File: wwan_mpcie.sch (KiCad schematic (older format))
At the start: 39 parts, among them J1501 u.FL, J1502 u.FL, J1503 MPCIE-Socket, J1504 Mini_SIM_Card, Q1501 FDV301N, SW1501 WWAN_HKS, U1501 NTB0104GU12, U1502 NUP5120, U1503 74LVC1G08

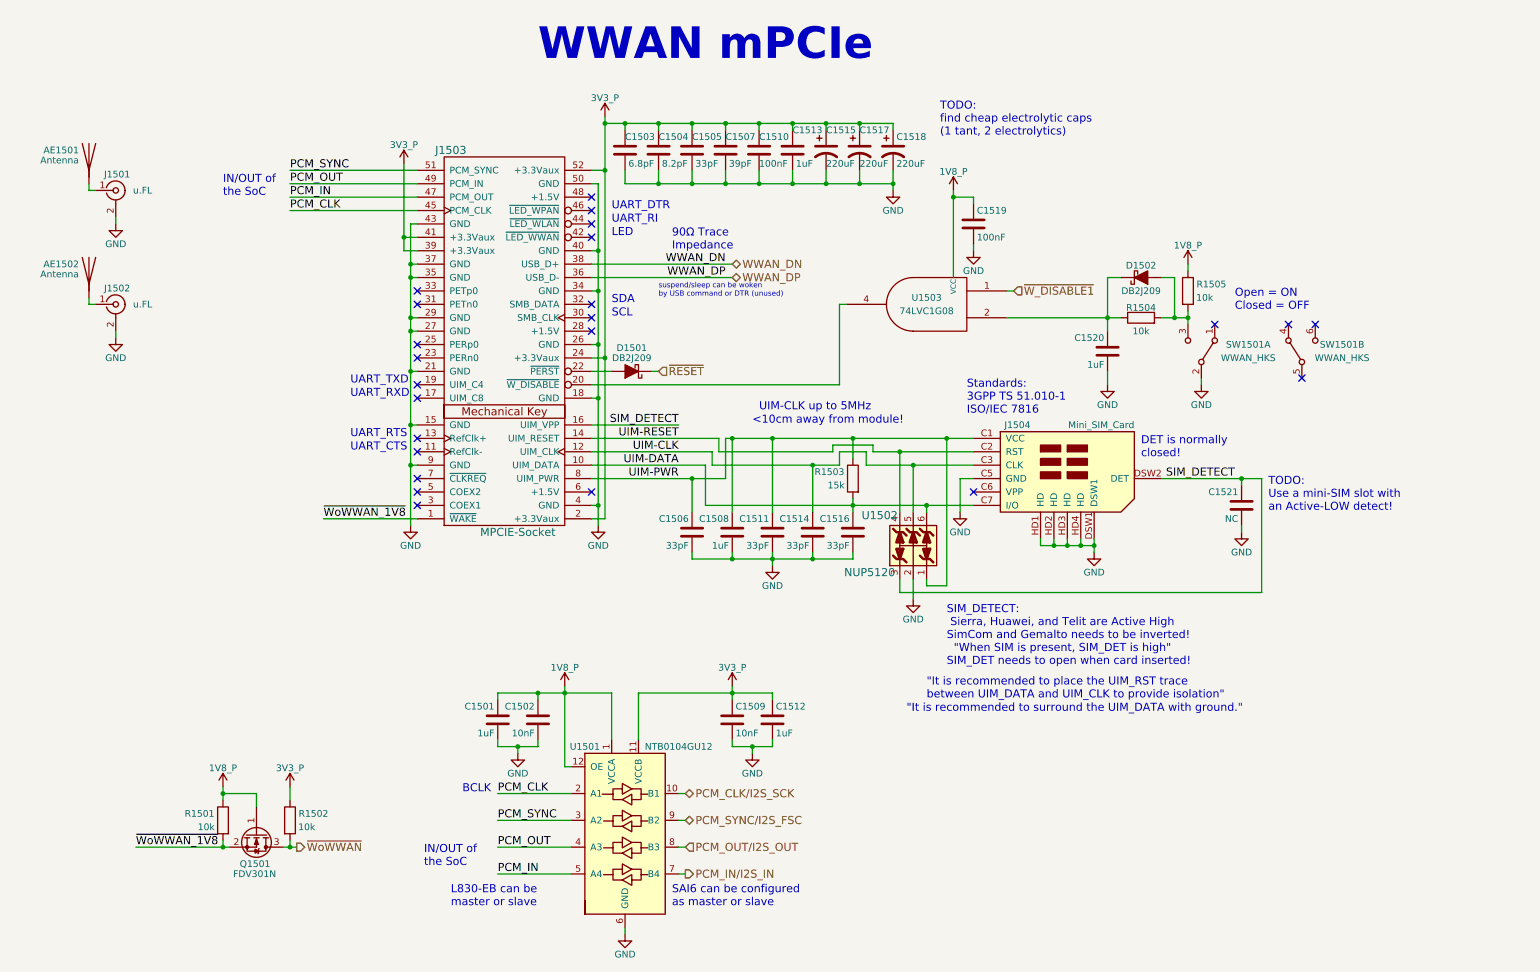
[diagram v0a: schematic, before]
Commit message: Added additional XOR gate to the WWAN page. This makes it possible that the polarity of the SIM_DETECT signal is configurable by one single O-Ohm-resistor. This adds more flexibility concerning modem choice, as there are both polarities of this signal used by different modem manufacturers. Added placeholder symbol for modem card (which holds now datasheet/bom information). The MPCIE socket has datasheet information, too. Picked two electrolytic capacitors (220uF/10V) by Panasonic by distributor TME.
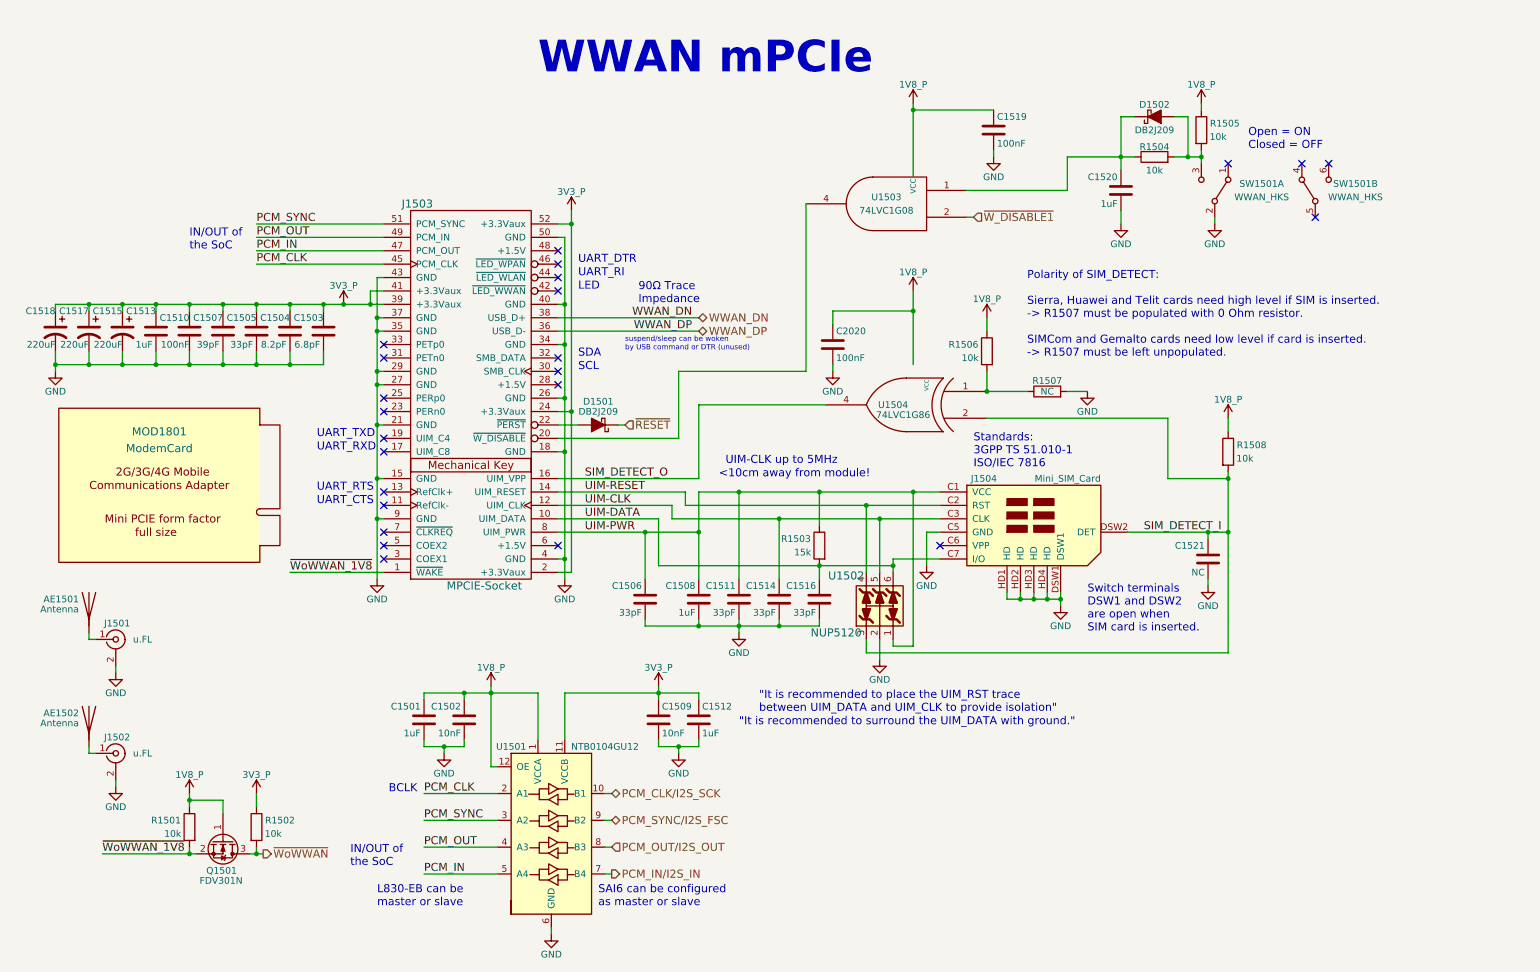
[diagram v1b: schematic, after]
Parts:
- added C2020: 100nF, Capacitors_SMD:C_0603, symbol C
- added MOD1801: ModemCard, symbol ModemCard
- added R1506, R1508: 10k, Resistors_SMD:R_0603, symbol R
- added R1507: NC, Resistors_SMD:R_0603, symbol R
- added U1504: 74LVC1G86, dvk-mx8m-bsb:74LVC1G86, symbol 74LVC1G86
- C1517, C1518: footprint Capacitors_Tantalum_SMD:CP_Tantalum_Case-D_EIA-7343-31_Reflow -> Capacitors_SMD:CP_Elec_6.3x7.7; Distrib Link https://www.tme.eu/en/details/tpsd227k010r010/smd-tantalum-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 -> https://www.tme.eu/en/details/eeefpa221xap/smd-low-imp-elec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; Distrib PN TPSD227K010R0100 -> EEEFPA221XAP; MFG Name AVX -> Panasonic; MFG Part Num TPSD227K010R0100 -> EEEFPA221XAP; Others https://www.arrow.com/en/products/293d227x9010d2te3/vishay -> http://uk.farnell.com/panasonic-electronic-components/eeefp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; Tolerance 10% -> +-20%
- J1503: Distrib Link (none) -> https://www2.mouser.com/ProductDetail/TE-Connectivity/20411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; MFG Name (none) -> TE Connectivity; MFG Part Number (none) -> 2041119-1
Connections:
- net 1V8_P: now also C2020.1, R1506.1, R1508.1
- net GND: now also C2020.2, R1507.2, U1504.3 (GND)
- net ~W_DISABLE1: now also U1503.2; no longer U1503.1
- net at C1520.1, D1502.1 (K), R1504.1: now also U1503.1; no longer U1503.2
- net SIM_DETECT renamed SIM_DETECT_I
- net SIM_DETECT_I: now also R1508.2, U1504.2; no longer J1503.16 (UIM_VPP)
- new net: R1506.2, R1507.1, U1504.1
- new net SIM_DETECT_O: J1503.16 (UIM_VPP), U1504.4
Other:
- note added: "Polarity of SIM_DETECT:\n\nSierra, Huawei and Telit cards need high level if SIM is inserted. \n-> R1507 must be populated with 0 Ohm resistor.\n\nSIMCom and Gemalto cards need low level if card is inserted.\n-> R1507 must be left unpopulated."
- note added: "Switch terminals\nDSW1 and DSW2\nare open when\nSIM card is inserted."
- note removed: "DET is normally \nclosed!"
- note removed: "SIM_DETECT:\n Sierra, Huawei, and Telit are Active High\nSimCom and Gemalto needs to be inverted!\n "When SIM is present, SIM_DET is high"\nSIM_DET needs to open when card inserted!"
- note removed: "TODO:\nUse a mini-SIM slot with\nan Active-LOW detect!"
- note removed: "TODO:\nfind cheap electrolytic caps\n(1 tant, 2 electrolytics)"
- moved on the sheet: AE1501, AE1502, C1501, C1502, C1503, C1504, C1505, C1506, C1507, C1508, C1509, C1510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

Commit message: Update WWAN mPCIe sheet by organizing a few things and fixing the component properties order
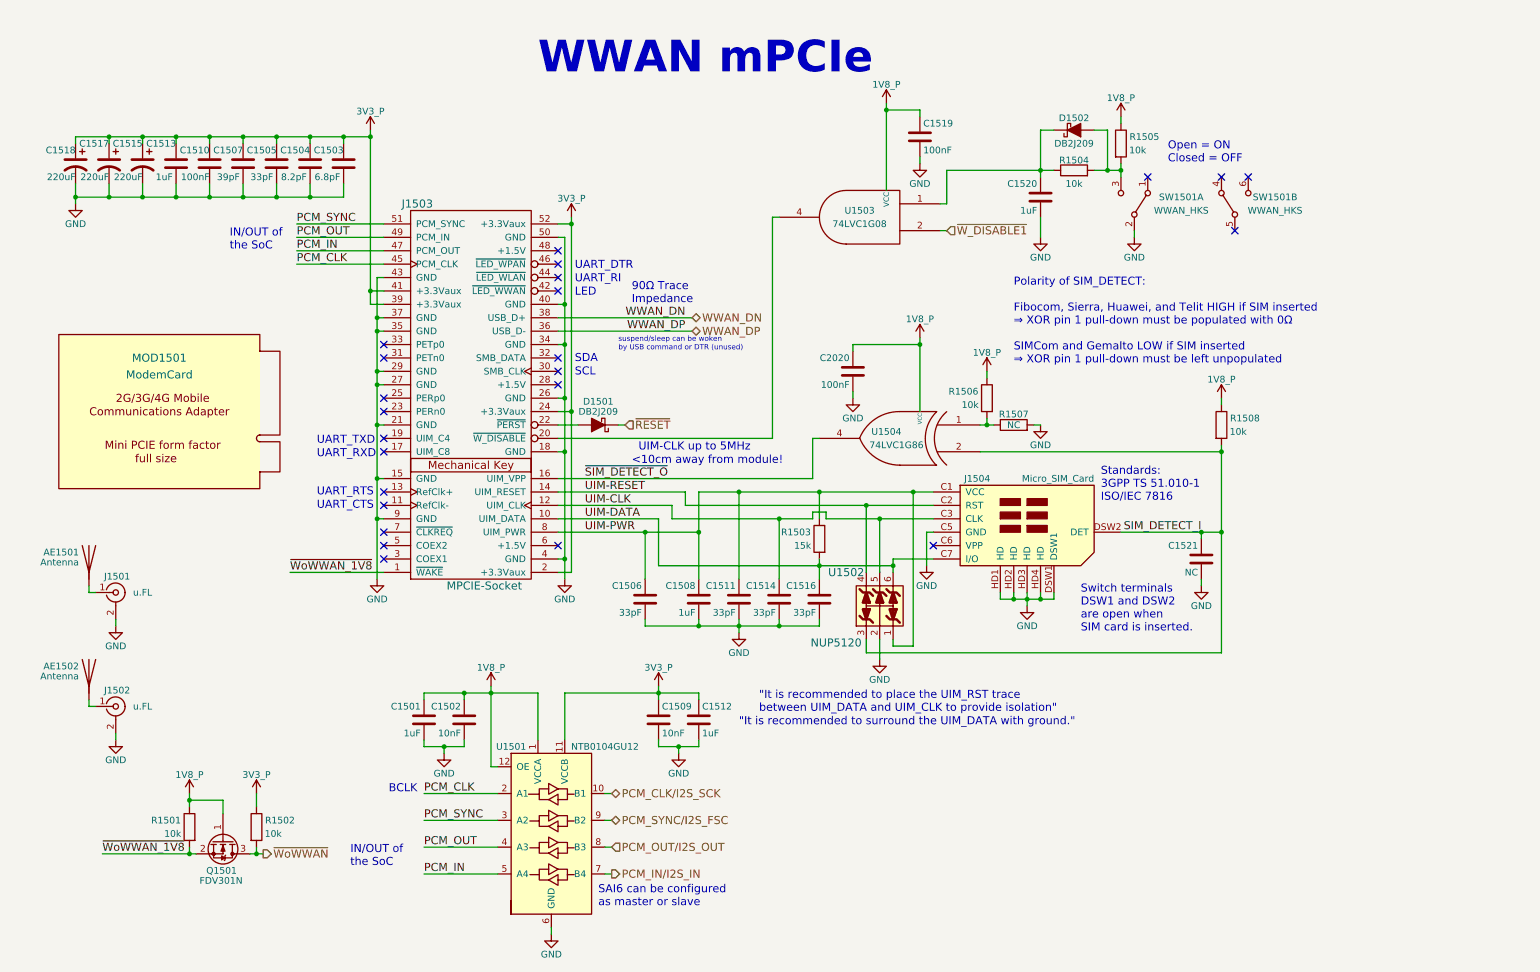
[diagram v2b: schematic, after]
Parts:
- C1517, C1518: Tolerance +-20% -> 20%
- J1503: Distrib PN (none) -> 571-2041119-1
- J1504: value Mini_SIM_Card -> Micro_SIM_Card
- U1503: DIstrib Link https://www.rocelec.com/part/nexnxp74lvc1g08gv125 -> (none); DIstrib PN (none) -> 74LVC1G08GV125; Distrib Link (none) -> https://www.rocelec.com/part/nexnxp74lvc1g08gv125
- U1504: Distrib PN (none) -> 74LVC1G86GV125; Tolerance (none) -> -
- renumbered MOD1801 to MOD1501
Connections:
- net 1V8_P: now also U1504.5 (VCC)
- net SIM_DETECT_O renamed ~SIM_DETECT_O
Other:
- note added: "Polarity of SIM_DETECT:\n\nFibocom, Sierra, Huawei, and Telit HIGH if SIM inserted\n⇒ XOR pin 1 pull-down must be populated with 0Ω\n\nSIMCom and Gemalto LOW if SIM inserted\n⇒ XOR pin 1 pull-down must be left unpopulated"
- note removed: "L830-EB can be\nmaster or slave"
- note removed: "Polarity of SIM_DETECT:\n\nSierra, Huawei and Telit cards need high level if SIM is inserted. \n-> R1507 must be populated with 0 Ohm resistor.\n\nSIMCom and Gemalto cards need low level if card is inserted.\n-> R1507 must be left unpopulated."
- moved on the sheet: AE1501, AE1502, C1503, C1504, C1505, C1507, C1510, C1513, C1515, C1517, C1518, C1519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

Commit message: Replace logic gate packages with cheaper options, change associated footprints to ones which match the cheaper alternatives
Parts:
- R1504, R1505: value 10k -> 100k
- U1503: footprint dvk-mx8m-bsb:74LVC1G08 -> dvk-mx8m-bsb:74LVC1G08GF; DIstrib PN 74LVC1G08GV125 -> 74LVC1G08GF/S505125; Distrib Link https://www.rocelec.com/part/nexnxp74lvc1g08gv125 -> https://www.rocelec.com/part/nexnxp74lvc1g08gf-s505125; MFG Part Num 74LVC1G08GV,125 -> 74LVC1G08GF
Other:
- note added: "Input pins are\ninterchangeable"
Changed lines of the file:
@@
 P 8800 1550
 F 0 "R1505" H 8975 1600 50  0000 C CNN
-F 1 "10k" H 8925 1500 50  0000 C CNN
+F 1 "100k" H 8950 1500 50  0000 C CNN
 F 2 "Resistors_SMD:R_0603" V 8730 1550 50  0001 C CNN
 F 3 "https://www.seielect.com/Catalog/SEI-RMCF_RMCP.pdf" H 8800 1550 50  0001 C CNN
@@
 P 8450 1750
 F 0 "R1504" V 8525 1750 50  0000 C CNN
-F 1 "10k" V 8350 1750 50  0000 C CNN
+F 1 "100k" V 8350 1750 50  0000 C CNN
 F 2 "Resistors_SMD:R_0603" V 8380 1750 50  0001 C CNN
 F 3 "https://www.seielect.com/Catalog/SEI-RMCF_RMCP.pdf" H 8450 1750 50  0001 C CNN
@@
 F 0 "U1503" H 6850 2150 50  0000 C CNN
 F 1 "74LVC1G08" H 6850 2050 50  0000 C CNN
-F 2 "dvk-mx8m-bsb:74LVC1G08" H 6850 2100 50  0001 C CNN
+F 2 "dvk-mx8m-bsb:74LVC1G08GF" H 6850 2100 50  0001 C CNN
 F 3 "https://assets.nexperia.com/documents/data-sheet/74LVC1G08.pdf" H 6850 2100 50  0001 C CNN
 F 4 "NXP" H 6850 2100 60  0001 C CNN "MFG Name"
-F 5 "74LVC1G08GV,125" H 6850 2100 60  0001 C CNN "MFG Part Num"
-F 6 "74LVC1G08GV125" H 6850 2100 60  0001 C CNN "DIstrib PN"
-F 7 "https://www.rocelec.com/part/nexnxp74lvc1g08gv125" H 6850 2100 60  0001 C CNN "Distrib Link"
+F 5 "74LVC1G08GF" H 6850 2100 60  0001 C CNN "MFG Part Num"
+F 6 "74LVC1G08GF/S505125" H 6850 2100 60  0001 C CNN "DIstrib PN"
+F 7 "https://www.rocelec.com/part/nexnxp74lvc1g08gf-s505125" H 6850 2100 60  0001 C CNN "Distrib Link"
 F 8 "-" H 6850 2100 60  0001 C CNN "Tolerance"
 F 9 "https://octopart.com/search?q=74LVC1G08GV%2C125&oq=74LVC1G08GV%2C125&start=0" H 6850 2100 60  0001 C CNN "Others"
@@
 	6900 5250 6900 5350
 Wire Wire Line
-	9550 5350 6900 5350
-Wire Wire Line
-	9550 3800 9550 5350
+	6900 5350 9550 5350
+Wire Wire Line
+	9550 5350 9550 3800
 Connection ~ 7000 4350
 Wire Wire Line
-	7250 4150 7250 5300
+	7250 5300 7250 4150
 Connection ~ 7250 4150
 Connection ~ 6900 4250
@@
 Wire Wire Line
 	8100 4900 8100 5000
+Text Notes 8350 3850 0    60   ~ 0
+Input pins are\ninterchangeable
+Text Notes 6300 1850 0    60   ~ 0
+Input pins are\ninterchangeable
 $EndSCHEMATC

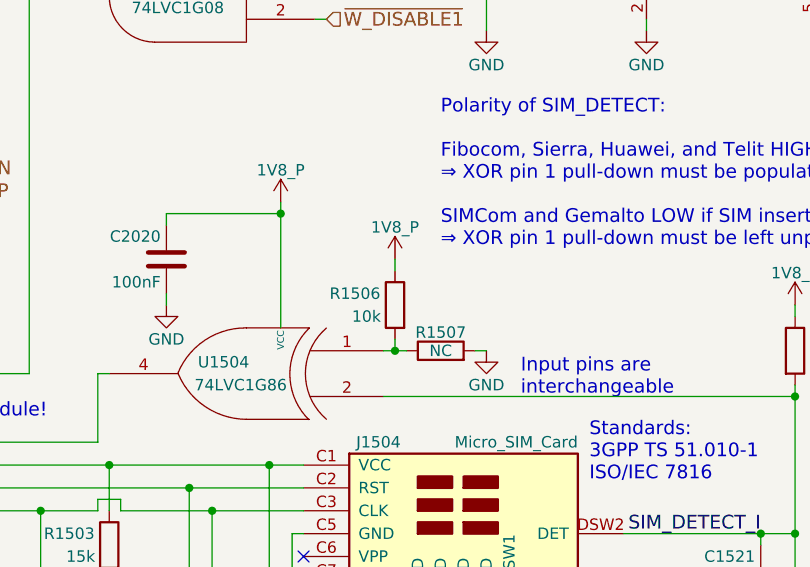
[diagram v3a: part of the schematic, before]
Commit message: Add WLAN+BT antenna component information
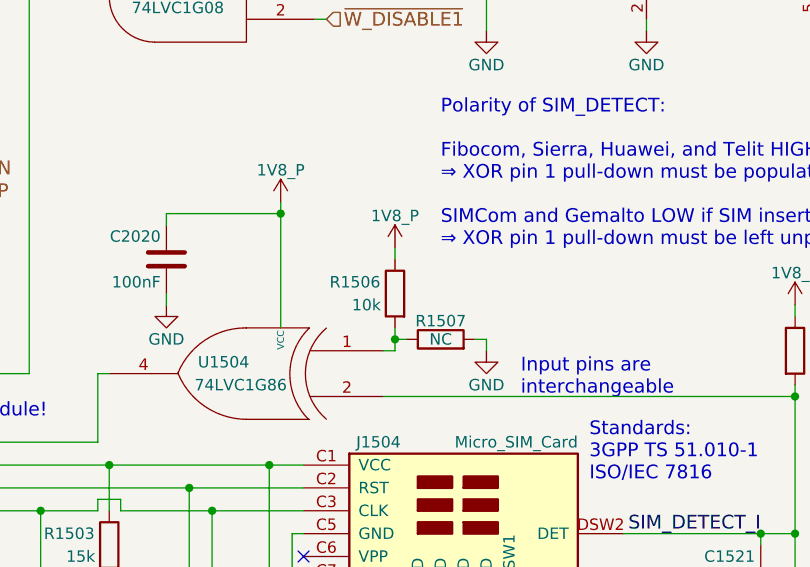
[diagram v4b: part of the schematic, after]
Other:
- moved on the sheet: R1506, R1507
